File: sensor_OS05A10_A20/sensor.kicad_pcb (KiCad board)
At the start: 4 copper layers, 49.8 x 49.8 mm, 41 parts, among them J1 FH35C-25S, U1 LP2985-2.8, U2 LP2985-1.8, U3 LP2985-1.2, U4 OS05A10-SMU

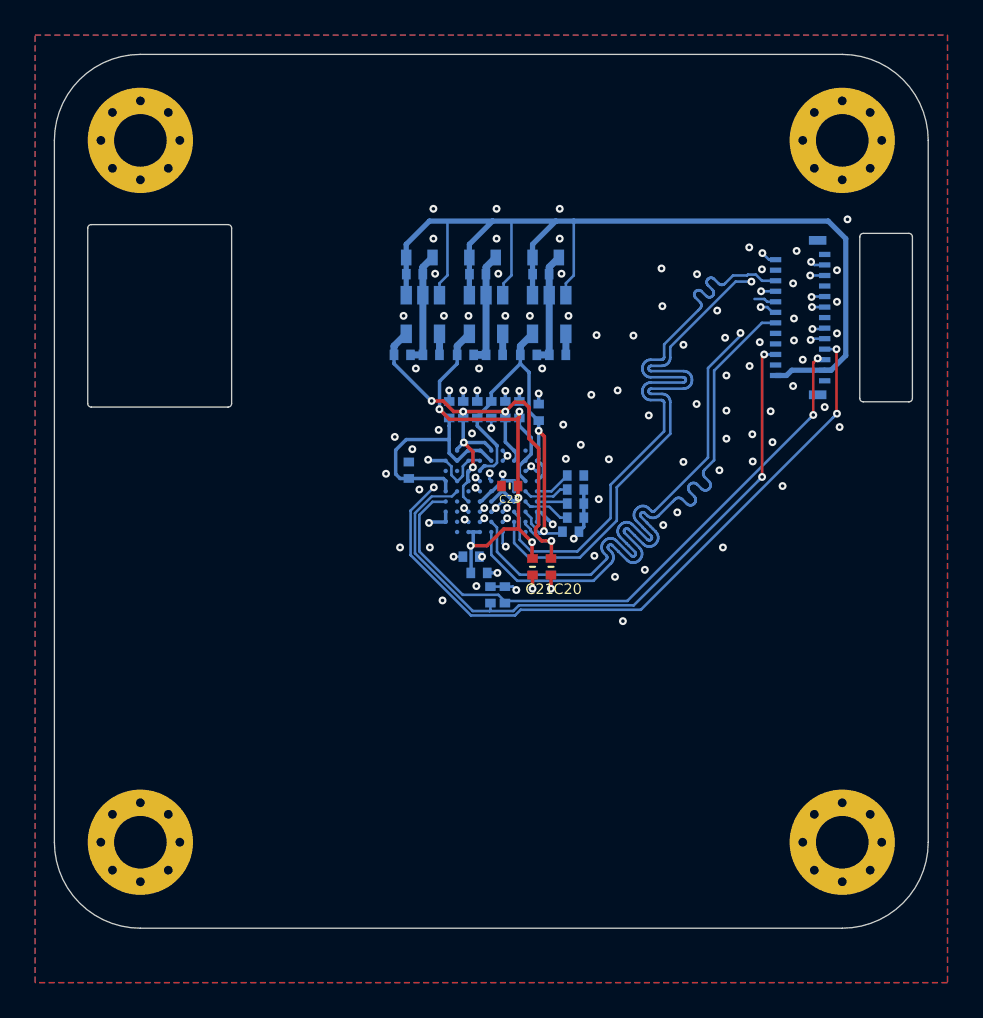
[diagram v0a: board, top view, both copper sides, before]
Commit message: updated to kicad 6
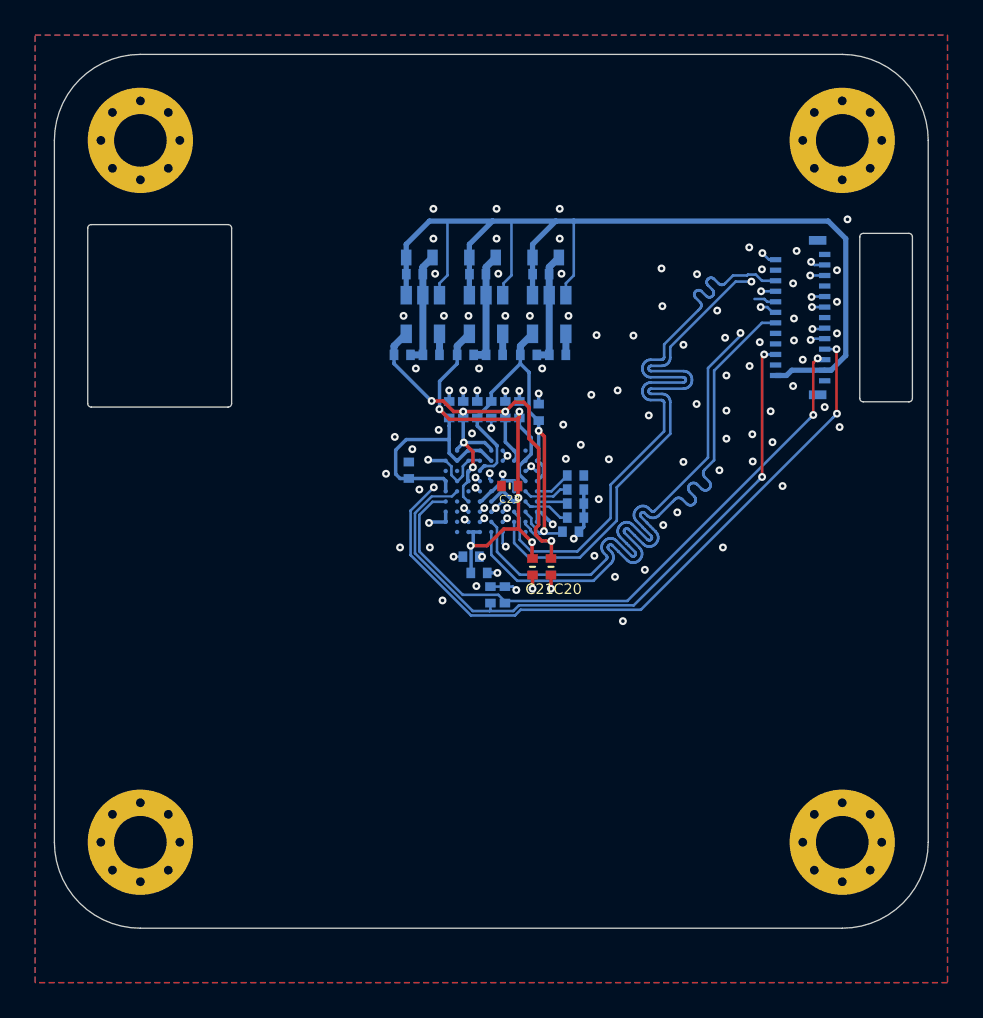
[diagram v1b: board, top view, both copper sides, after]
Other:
- net class Default removed
- board text added: "OtterCam-s3 OS05A10/20 Board Jana Marie Hemsing @_Jana_Marie 2022 rev 1.11 github.com/Jana-Marie/OtterCam-s3"
- board text removed: "OtterCam-s3 OS05A10/20 Board Jana Marie Hemsing @JanHenrikH 2021 rev 1.1 github.com/Jana-Marie/OtterCam-s3"

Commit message: updated sensor board
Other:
- board text added: "OtterCam-s3 OS05A10/20 Board Jana Marie Hemsing @jana@mystical.garden 2023 rev 1.11.1 github.com/Jana-Marie/OtterCam-s3"
- board text removed: "OtterCam-s3 OS05A10/20 Board Jana Marie Hemsing @_Jana_Marie 2022 rev 1.11 github.com/Jana-Marie/OtterCam-s3"
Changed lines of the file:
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@@
       (drillshape 0)
       (scaleselection 1)
-      (outputdirectory "gerber_v1.1/")
+      (outputdirectory "gerber_v1.1.1/")
     )
   )
@@
   (gr_line (start 98.8 60.3) (end 96.2 60.3) (layer "Edge.Cuts") (width 0.05))
   (gr_arc (start 98.8 60.3) (mid 98.941421 60.358579) (end 99 60.5) (layer "Edge.Cuts") (width 0.05))
-  (gr_text "OtterCam-s3 OS05A10/20 Board\nJana Marie Hemsing\n@_Jana_Marie 2022 rev 1.11\ngithub.com/Jana-Marie/OtterCam-s3" (at 75 92) (layer "B.SilkS")
+  (gr_text "OtterCam-s3 OS05A10/20 Board\nJana Marie Hemsing\n@jana@mystical.garden 2023 rev 1.11.1\ngithub.com/Jana-Marie/OtterCam-s3" (at 75 92) (layer "B.SilkS")
     (effects (font (size 1.1 1.1) (thickness 0.13)) (justify mirror))
   )
